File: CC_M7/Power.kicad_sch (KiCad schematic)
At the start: 15 parts, among them U10 ME6211C33M5, U8 TPS54202DDCR, U9 ME6211C33M5

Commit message: IIM42652 schematic added
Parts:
- C48: footprint Capacitor_SMD:C_0402_1005Metric -> Capacitor_SMD:C_0603_1608Metric
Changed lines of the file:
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@@
 			)
 		)
-		(property "Footprint" "Capacitor_SMD:C_0402_1005Metric"
+		(property "Footprint" "Capacitor_SMD:C_0603_1608Metric"
 			(at 129.2352 46.99 0)
 			(effects

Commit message: assigned footprint completed
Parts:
- L5: footprint (none) -> Inductor_SMD:L_0603_1608Metric
- R10, R12, R13: footprint (none) -> Resistor_SMD:R_0805_2012Metric
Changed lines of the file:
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@@
 			)
 		)
-		(property "Footprint" ""
+		(property "Footprint" "Inductor_SMD:L_0603_1608Metric"
 			(at 119.38 38.1 0)
 			(effects
@@
 			)
 		)
-		(property "Footprint" ""
+		(property "Footprint" "Resistor_SMD:R_0805_2012Metric"
 			(at 140.208 54.61 90)
 			(effects
@@
 			)
 		)
-		(property "Footprint" ""
+		(property "Footprint" "Resistor_SMD:R_0805_2012Metric"
 			(at 162.56 39.878 90)
 			(effects
@@
 			)
 		)
-		(property "Footprint" ""
+		(property "Footprint" "Resistor_SMD:R_0805_2012Metric"
 			(at 140.208 44.45 90)
 			(effects

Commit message: ready to start PCB drawing
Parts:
- removed C43: 22uF, Capacitor_SMD:C_1210_3225Metric, symbol Device:C
- removed C47: 100nF, Capacitor_SMD:C_1210_3225Metric, symbol Device:C
- removed C48: 68pF, Capacitor_SMD:C_0603_1608Metric, symbol Device:C
- removed C49: 47uF, Capacitor_SMD:C_1210_3225Metric, symbol Device:C
- removed L5: 10uH, Inductor_SMD:L_0603_1608Metric, symbol Device:L
- removed R10: 0R, Resistor_SMD:R_0805_2012Metric, symbol Device:R
- removed R12: 100k, Resistor_SMD:R_0805_2012Metric, symbol Device:R
- removed R13: 13.7k, Resistor_SMD:R_0805_2012Metric, symbol Device:R
- removed U8: TPS54202DDCR, TPS54202DDCR:SOT95P280X110-6N, symbol TPS54202DDCR:TPS54202DDCR
- added C43, C57: 10uF, Capacitor_SMD:C_0805_2012Metric, symbol Device:C_Small
- added C47, C48: 100nF, Capacitor_SMD:C_0603_1608Metric, symbol Device:C_Small
- added C49: 47pF, Capacitor_SMD:C_0603_1608Metric, symbol Device:C_Small
- added C56: 22uF, Capacitor_SMD:C_0805_2012Metric, symbol Device:C_Small
- added L3: 3.3uH, Inductor_SMD:L_Changjiang_FXL0650, symbol Device:L_Small
- added R10: 100K, Resistor_SMD:R_0603_1608Metric, symbol Device:R_Small
- added R12: 220K, Resistor_SMD:R_0603_1608Metric, symbol Device:R_Small
- added R13: 30K, Resistor_SMD:R_0603_1608Metric, symbol Device:R_Small
- added U8: TPS562246DRLR, TPS562246DRLR:DRL0006A-MFG, symbol 2025-02-12_17-10-08:TPS562246DRLR
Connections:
- net GND: now also C43.1, C47.1, C56.1, C57.1, R13.2, U8.3 (GND)
- new net: C48.1, C49.2, L3.1, U8.2 (SW)
- new net: C48.2, U8.4 (BST)
- new net: R10.1, U8.5 (EN)
- new net: C49.1, R12.2, R13.1, U8.6 (FB)
- new net: C56.2, L3.2, R12.1
- new net +BATT: C43.2, C47.2, C57.2, R10.2, U8.1 (VIN)
- no-connect marks 1 -> 0
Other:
- note added: "TPS562242DRLR"
- note removed: "DEVRE KONTROL EDILECEK!!!!!"
- note removed: "TPS54202DDCR"

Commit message: Schematic pdf added.
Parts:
- added J13: Batt_Pins, Connector_Molex:Molex_KK-254_AE-6410-02A_1x02_P2.54mm_Vertical, symbol Connector:Conn_01x02_Pin
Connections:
- net +BATT: now also J13.1 (Pin_1)
- net GND: now also J13.2 (Pin_2)
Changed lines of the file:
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@@
+	(wire
+		(pts
+			(xy 40.64 187.96) (xy 46.355 187.96)
+		)
+		(stroke
+			(width 0)
+			(type default)
+		)
+	)
 	(wire
 		(pts
@@
 	(wire
 		(pts
+			(xy 46.355 187.96) (xy 46.355 189.865)
+		)
+		(stroke
+			(width 0)
+			(type default)
+		)
+	)
+	(wire
+		(pts
 			(xy 125.73 138.43) (xy 125.73 140.97)
 		)
@@
 	(wire
 		(pts
+			(xy 46.355 185.42) (xy 46.355 183.515)
+		)
+		(stroke
+			(width 0)
+			(type default)
+		)
+	)
+	(wire
+		(pts
 			(xy 66.04 127) (xy 74.93 127)
 		)
@@
 		(pts
 			(xy 125.73 125.73) (xy 125.73 128.27)
+		)
+		(stroke
+			(width 0)
+			(type default)
+		)
+	)
+	(wire
+		(pts
+			(xy 40.64 185.42) (xy 46.355 185.42)
 		)
 		(stroke
@@
 	)
 	(symbol
+		(lib_id "power:+BATT")
+		(at 46.355 183.515 0)
+		(unit 1)
+		(exclude_from_sim no)
+		(in_bom yes)
+		(on_board yes)
+		(dnp no)
+		(fields_autoplaced yes)
+		(property "Reference" "#PWR0107"
+			(at 46.355 187.325 0)
+			(effects
+				(font
+					(size 1.27 1.27)
+				)
+				(hide yes)
+			)
+		)
+		(property "Value" "+BATT"
+			(at 46.355 178.435 0)
+			(effects
+				(font
+					(size 1.27 1.27)
+				)
+			)
+		)
+		(property "Footprint" ""
+			(at 46.355 183.515 0)
+			(effects
+				(font
+					(size 1.27 1.27)
+				)
+				(hide yes)
+			)
+		)
+		(property "Datasheet" ""
+			(at 46.355 183.515 0)
+			(effects
+				(font
+					(size 1.27 1.27)
+				)
+				(hide yes)
+			)
+		)
+		(property "Description" "Power symbol creates a global label with name \"+BATT\""
+			(at 46.355 183.515 0)
+			(effects
+				(font
+					(size 1.27 1.27)
+				)
+				(hide yes)
+			)
+		)
+		(pin "1"
+		)
+		(instances
+			(project "CC_M7"
+				(path "/20c3bbae-00c6-470e-8b69-dc0f665257a3/d5e2a406-9a7f-4b4d-9070-1dc6f1aabbf7"
+					(reference "#PWR0107")
+					(unit 1)
+				)
+			)
+		)
+	)
+	(symbol
+		(lib_id "Connector:Conn_01x02_Pin")
+		(at 35.56 185.42 0)
+		(unit 1)
+		(exclude_from_sim no)
+		(in_bom yes)
+		(on_board yes)
+		(dnp no)
+		(fields_autoplaced yes)
+		(property "Reference" "J13"
+			(at 36.195 180.975 0)
+			(effects
+				(font
+					(size 1.27 1.27)
+				)
+			)
+		)
+		(property "Value" "Batt_Pins"
+			(at 36.195 183.515 0)
+			(effects
+				(font
+					(size 1.27 1.27)
+				)
+			)
+		)
+		(property "Footprint" "Connector_Molex:Molex_KK-254_AE-6410-02A_1x02_P2.54mm_Vertical"
+			(at 35.56 185.42 0)
+			(effects
+				(font
+					(size 1.27 1.27)
+				)
+				(hide yes)
+			)
+		)
+		(property "Datasheet" "~"
+			(at 35.56 185.42 0)
+			(effects
+				(font
+					(size 1.27 1.27)
+				)
+				(hide yes)
+			)
+		)
+		(property "Description" "Generic connector, single row, 01x02, script generated"
+			(at 35.56 185.42 0)
+			(effects
+				(font
+					(size 1.27 1.27)
+				)
+				(hide yes)
+			)
+		)
+		(pin "2"
+		)
+		(pin "1"
+		)
+		(instances
+			(project ""
+				(path "/20c3bbae-00c6-470e-8b69-dc0f665257a3/d5e2a406-9a7f-4b4d-9070-1dc6f1aabbf7"
+					(reference "J13")
+					(unit 1)
+				)
+			)
+		)
+	)
+	(symbol
 		(lib_id "power:GND")
 		(at 140.97 140.97 0)
@@
 					(unit 1)
 				)
+			)
+		)
+	)
+	(symbol
+		(lib_id "power:GND")
+		(at 46.355 189.865 0)
+		(unit 1)
+		(exclude_from_sim no)
+		(in_bom yes)
+		(on_board yes)
+		(dnp no)
+		(fields_autoplaced yes)
+		(property "Reference" "#PWR0108"
+			(at 46.355 196.215 0)
+			(effects
+				(font
+					(size 1.27 1.27)
+				)
+				(hide yes)
+			)
+		)
+		(property "Value" "GND"
+			(at 46.355 194.945 0)
+			(effects
+				(font
+					(size 1.27 1.27)
+				)
+			)
+		)
+		(property "Footprint" ""
+			(at 46.355 189.865 0)
+			(effects
+				(font
+					(size 1.27 1.27)
+				)
+				(hide yes)
+			)
+		)
+		(property "Datasheet" ""
+			(at 46.355 189.865 0)
+			(effects
+				(font
+					(size 1.27 1.27)
+				)
+				(hide yes)
+			)
+		)
+		(property "Description" "Power symbol creates a global label with name \"GND\" , ground"
+			(at 46.355 189.865 0)
+			(effects
+				(font
+					(size 1.27 1.27)
+				)
+				(hide yes)
+			)
+		)
+		(pin "1"
+		)
+		(instances
+			(project "CC_M7"
+				(path "/20c3bbae-00c6-470e-8b69-dc0f665257a3/d5e2a406-9a7f-4b4d-9070-1dc6f1aabbf7"
+					(reference "#PWR0108")
+					(unit 1)
+				)

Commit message: [200~
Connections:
- net +5V: now also C56.2, L3.2, R12.1
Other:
- moved on the sheet: C56
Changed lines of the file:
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@@
+	)
+	(junction
+		(at 175.26 38.1)
+		(diameter 0)
+		(color 0 0 0 0)
 	)
 	(junction
@@
 	(wire
 		(pts
+			(xy 186.055 33.655) (xy 186.055 38.1)
+		)
+		(stroke
+			(width 0)
+			(type default)
+		)
+	)
+	(wire
+		(pts
 			(xy 68.58 38.1) (xy 73.66 38.1)
 		)
@@
 	(wire
 		(pts
+			(xy 175.26 45.72) (xy 175.26 46.355)
+		)
+		(stroke
+			(width 0)
+			(type default)
+		)
+	)
+	(wire
+		(pts
 			(xy 165.1 38.1) (xy 165.1 40.64)
 		)
@@
 	(wire
 		(pts
+			(xy 175.26 38.1) (xy 186.055 38.1)
+		)
+		(stroke
+			(width 0)
+			(type default)
+		)
+	)
+	(wire
+		(pts
 			(xy 43.18 127) (xy 50.8 127)
 		)
@@
 	(wire
 		(pts
-			(xy 165.1 38.1) (xy 180.34 38.1)
+			(xy 165.1 38.1) (xy 175.26 38.1)
 		)
 		(stroke
@@
 		(pts
 			(xy 140.97 138.43) (xy 140.97 140.97)
+		)
+		(stroke
+			(width 0)
+			(type default)
+		)
+	)
+	(wire
+		(pts
+			(xy 175.26 40.64) (xy 175.26 38.1)
 		)
 		(stroke
@@
 	(symbol
 		(lib_id "Device:C_Small")
-		(at 180.34 40.64 180)
+		(at 175.26 43.18 180)
 		(unit 1)
 		(exclude_from_sim no)
@@
 		(fields_autoplaced yes)
 		(property "Reference" "C56"
-			(at 182.88 39.3635 0)
+			(at 177.8 41.9035 0)
 			(effects
 				(font
@@
 		)
 		(property "Value" "22uF"
-			(at 182.88 41.9035 0)
+			(at 177.8 44.4435 0)
 			(effects
 				(font
@@
 		)
 		(property "Footprint" "Capacitor_SMD:C_0805_2012Metric"
-			(at 180.34 40.64 0)
+			(at 175.26 43.18 0)
 			(effects
 				(font
@@
 		)
 		(property "Datasheet" "~"
-			(at 180.34 40.64 0)
+			(at 175.26 43.18 0)
 			(effects
 				(font
@@
 		)
 		(property "Description" "Unpolarized capacitor, small symbol"
-			(at 180.34 40.64 0)
+			(at 175.26 43.18 0)
 			(effects
 				(font
@@
 	(symbol
 		(lib_id "power:GND")
-		(at 180.34 43.18 0)
+		(at 175.26 46.355 0)
 		(unit 1)
 		(exclude_from_sim no)
@@
 		(fields_autoplaced yes)
 		(property "Reference" "#PWR0100"
-			(at 180.34 49.53 0)
+			(at 175.26 52.705 0)
 			(effects
 				(font
@@
 		)
 		(property "Value" "GND"
-			(at 180.34 48.26 0)
+			(at 175.26 51.435 0)
 			(effects
 				(font
@@
 		)
 		(property "Footprint" ""
-			(at 180.34 43.18 0)
+			(at 175.26 46.355 0)
 			(effects
 				(font
@@
 		)
 		(property "Datasheet" ""
-			(at 180.34 43.18 0)
+			(at 175.26 46.355 0)
 			(effects
 				(font
@@
 		)
 		(property "Description" "Power symbol creates a global label with name \"GND\" , ground"
-			(at 180.34 43.18 0)
+			(at 175.26 46.355 0)
 			(effects
 				(font
@@
 					(unit 1)
 				)
+			)
+		)
+	)
+	(symbol
+		(lib_id "power:+5V")
+		(at 186.055 33.655 0)
+		(unit 1)
+		(exclude_from_sim no)
+		(in_bom yes)
+		(on_board yes)
+		(dnp no)
+		(fields_autoplaced yes)
+		(property "Reference" "#PWR0109"
+			(at 186.055 37.465 0)
+			(effects
+				(font
+					(size 1.27 1.27)
+				)
+				(hide yes)
+			)
+		)
+		(property "Value" "+5V"
+			(at 186.055 28.575 0)
+			(effects
+				(font
+					(size 1.27 1.27)
+				)
+			)
+		)
+		(property "Footprint" ""
+			(at 186.055 33.655 0)
+			(effects
+				(font
+					(size 1.27 1.27)
+				)
+				(hide yes)
+			)
+		)
+		(property "Datasheet" ""
+			(at 186.055 33.655 0)
+			(effects
+				(font
+					(size 1.27 1.27)
+				)
+				(hide yes)
+			)
+		)
+		(property "Description" "Power symbol creates a global label with name \"+5V\""
+			(at 186.055 33.655 0)
+			(effects
+				(font
+					(size 1.27 1.27)
+				)
+				(hide yes)
+			)
+		)
+		(pin "1"
+		)
+		(instances
+			(project "CC_M7"
+				(path "/20c3bbae-00c6-470e-8b69-dc0f665257a3/d5e2a406-9a7f-4b4d-9070-1dc6f1aabbf7"
+					(reference "#PWR0109")
+					(unit 1)
+				)

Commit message: PCB track draw.
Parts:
- added D1: MBR230LSFT1G, MBR230LSFT1G:SODFL3619X98N, symbol MBR230LSFT1G:MBR230LSFT1G
- added F1: Polyfuse, Fuse:Fuse_1206_3216Metric, symbol Device:Polyfuse
- C43, C57: footprint Capacitor_SMD:C_0805_2012Metric -> Capacitor_SMD:C_1206_3216Metric
- C47: footprint Capacitor_SMD:C_0603_1608Metric -> Capacitor_SMD:C_1206_3216Metric
- J13: footprint Connector_Molex:Molex_KK-254_AE-6410-02A_1x02_P2.54mm_Vertical -> Connector_PinSocket_2.54mm:PinSocket_1x02_P2.54mm_Vertical
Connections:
- net +5V: now also F1.2; no longer C56.2, L3.2, R12.1
- net +BATT: now also D1.A; no longer C43.2, C47.2, C57.2, R10.2, U8.1 (VIN)
- new net: C43.2, C47.2, C57.2, D1.K, R10.2, U8.1 (VIN)
- new net VIN_5V: C56.2, F1.1, L3.2, R12.1

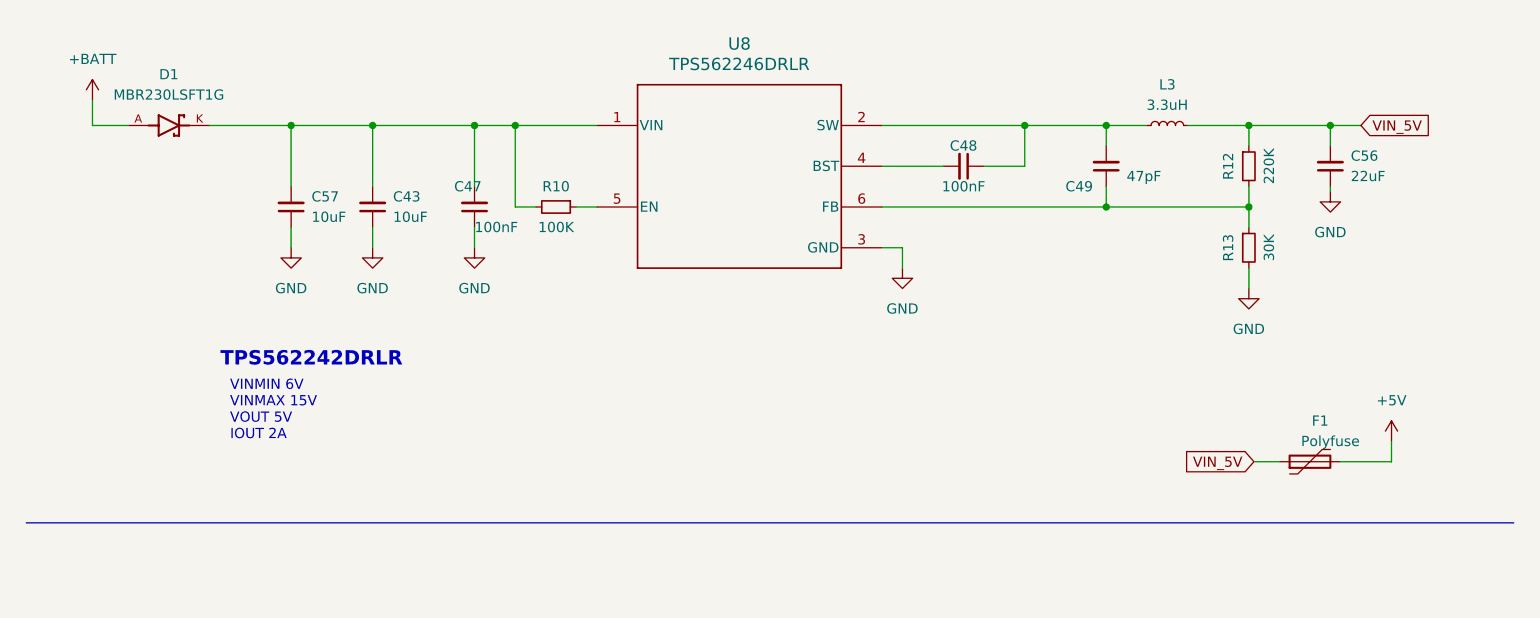
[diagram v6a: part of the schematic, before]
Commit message: Reverse current protection added. | Routing progress.
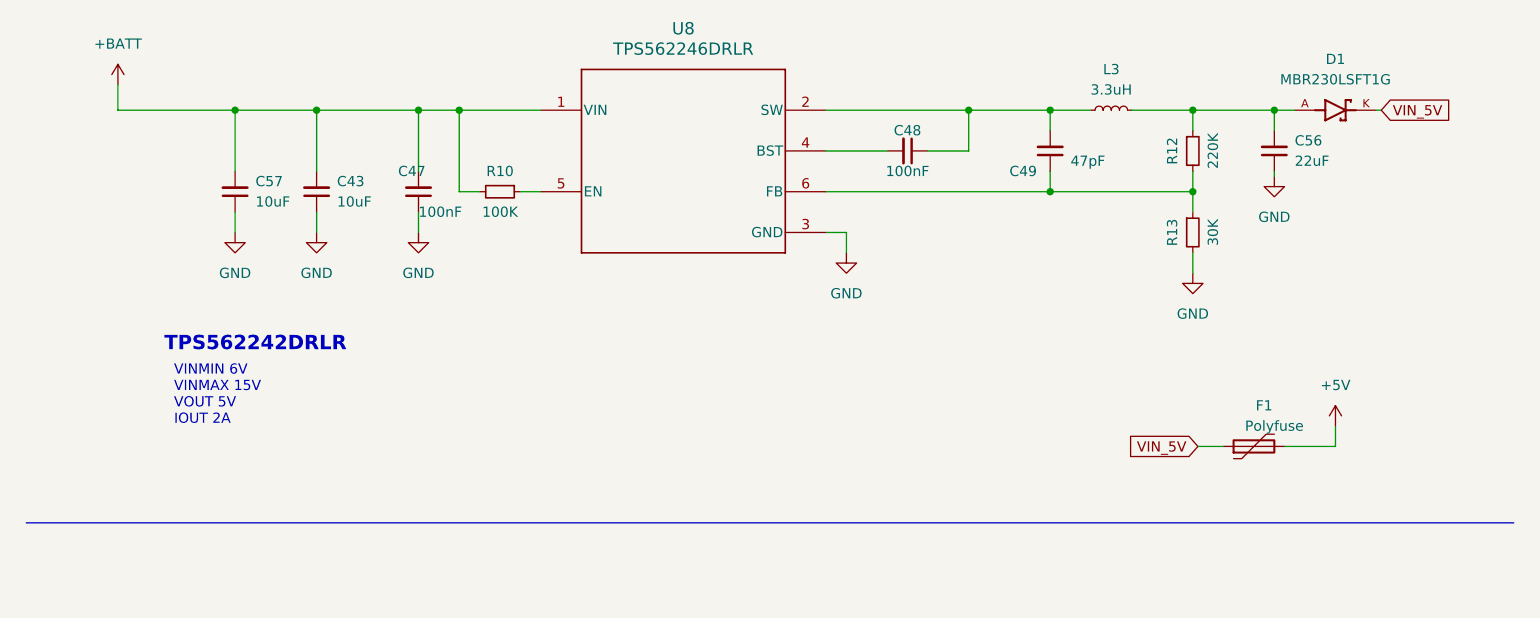
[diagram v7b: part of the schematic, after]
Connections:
- net +BATT: now also C43.2, C47.2, C57.2, R10.2, U8.1 (VIN); no longer D1.A
- net VIN_5V: now also D1.K; no longer C56.2, L3.2, R12.1
- new net: C56.2, D1.A, L3.2, R12.1
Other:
- moved on the sheet: C43, C47, C48, C49, C56, C57, F1, L3, R10, R12, R13, U8

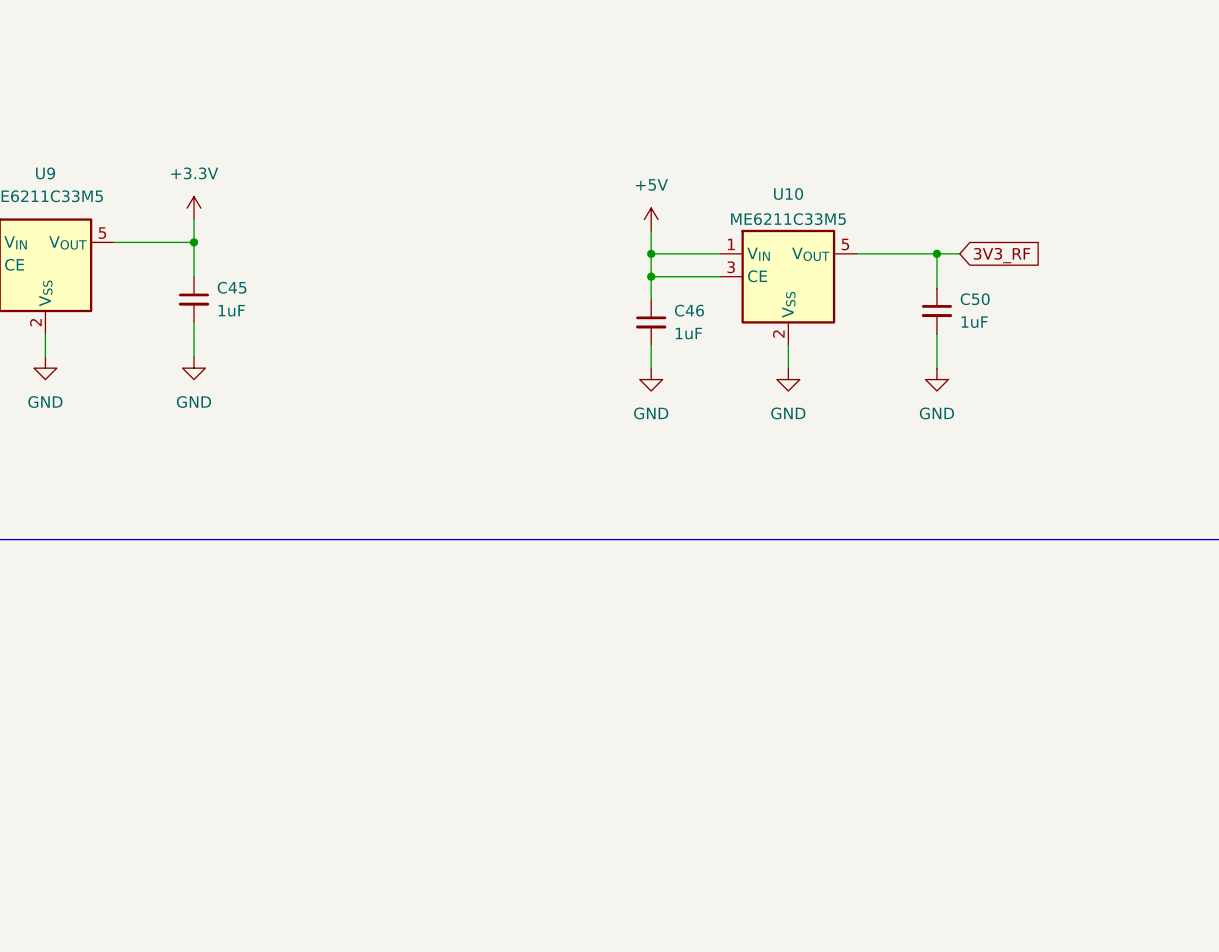
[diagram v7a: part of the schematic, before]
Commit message: Routing | Silkscreen Design Completed. | Power Led Added. | Schematic PDF deleted | Mounting Hole Pad Clearance added. | BMM150 Conneciton Fixed.
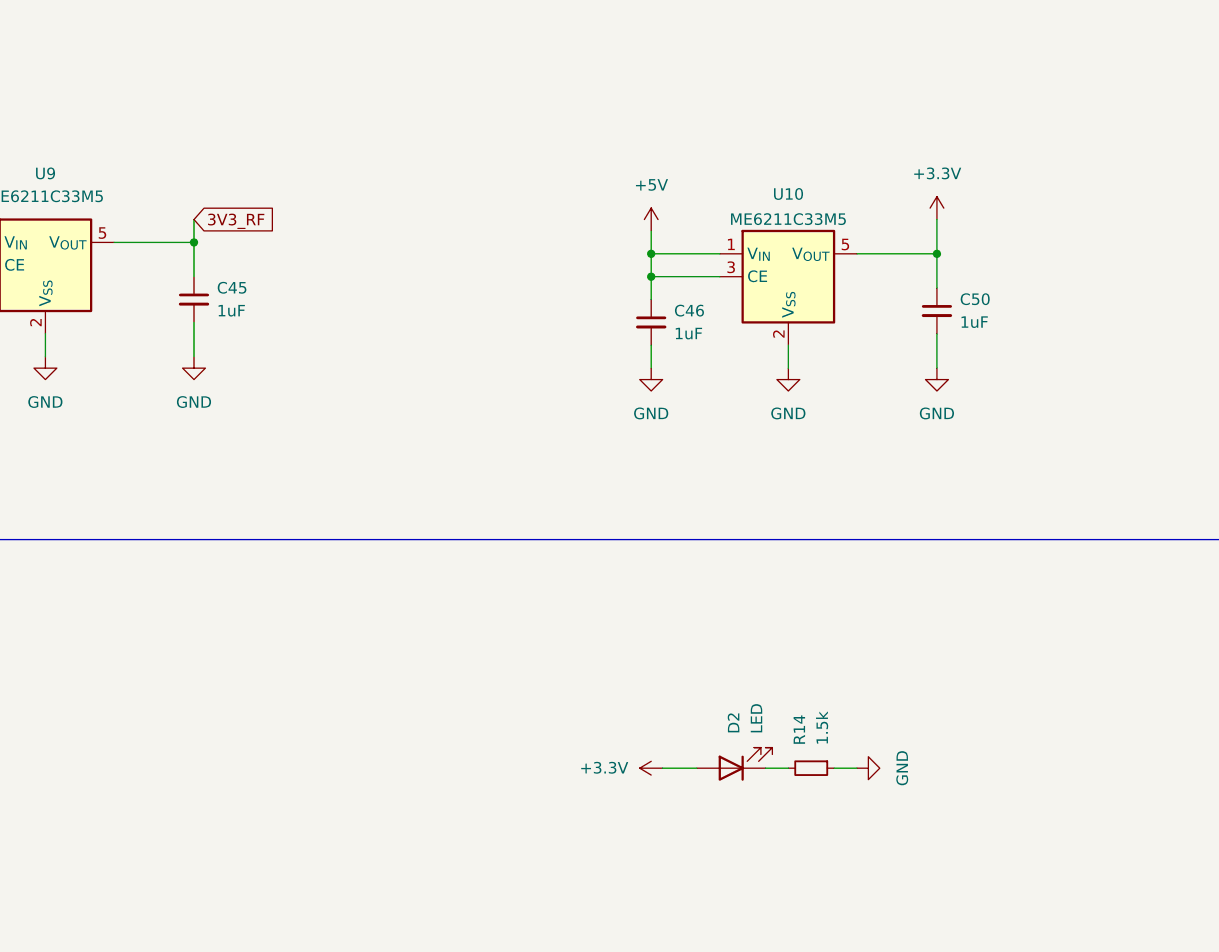
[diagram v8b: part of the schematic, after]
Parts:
- added D2: LED, LED_SMD:LED_0603_1608Metric, symbol Device:LED
- added R14: 1.5k, Resistor_SMD:R_0603_1608Metric, symbol Device:R_Small
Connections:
- net +3.3V: now also C50.1, U10.5 (V_{OUT}), D2.2 (A); no longer C45.1, U9.5 (V_{OUT})
- net 3V3_RF: now also C45.1, U9.5 (V_{OUT}); no longer C50.1, U10.5 (V_{OUT})
- net GND: now also R14.1
- new net: D2.1 (K), R14.2
